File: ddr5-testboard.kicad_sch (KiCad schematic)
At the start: 2 parts

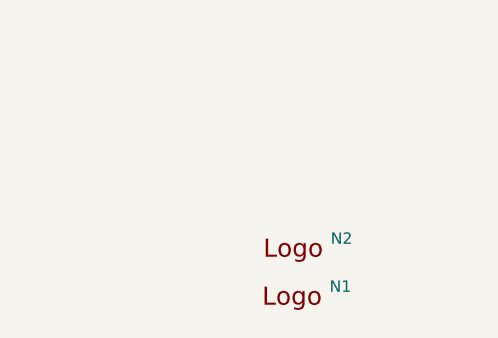
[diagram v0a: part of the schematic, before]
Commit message: Added EN pullup for TPS54561 to avoid disabling by touch
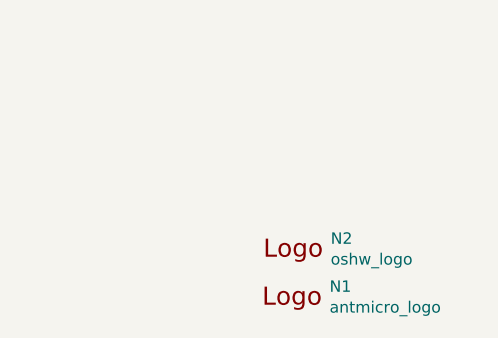
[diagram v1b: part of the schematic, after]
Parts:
- N1: value (none) -> antmicro_logo; footprint (none) -> ddr5-testboard-footprints:antmicro-logo_scaled_20mm
- N2: value (none) -> oshw_logo; footprint (none) -> ddr5-testboard-footprints:oshw-logo
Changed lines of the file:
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@@
       (effects (font (size 1.27 1.27)) (justify left))
     )
-    (property "Value" "" (id 1) (at 390.8806 248.2342 0)
+    (property "Value" "antmicro_logo" (id 1) (at 390.8806 248.2342 0)
       (effects (font (size 1.27 1.27)) (justify left))
     )
-    (property "Footprint" "" (id 2) (at 382.905 241.935 0)
+    (property "Footprint" "ddr5-testboard-footprints:antmicro-logo_scaled_20mm" (id 2) (at 382.905 241.935 0)
       (effects (font (size 1.27 1.27)) hide)
     )
@@
       (effects (font (size 1.27 1.27)) (justify left))
     )
-    (property "Value" "" (id 1) (at 391.0076 242.9002 0)
+    (property "Value" "oshw_logo" (id 1) (at 391.0076 242.9002 0)
       (effects (font (size 1.27 1.27)) (justify left))
     )
-    (property "Footprint" "" (id 2) (at 386.588 246.761 0)
+    (property "Footprint" "ddr5-testboard-footprints:oshw-logo" (id 2) (at 386.588 246.761 0)
       (effects (font (size 1.27 1.27)) hide)
     )
@@
       (reference "R142") (unit 1) (value "R_0R_0402") (footprint "ddr5-testboard-footprints:0402-res")
     )
+    (path "/00000000-0000-0000-0000-000060225b0c/74b36243-a924-4abe-ab54-890d809b0794"
+      (reference "R143") (unit 1) (value "R_243k_0402") (footprint "ddr5-testboard-footprints:0402-res")
+    )
     (path "/00000000-0000-0000-0000-000061b4860c/00000000-0000-0000-0000-00006227af2e"
